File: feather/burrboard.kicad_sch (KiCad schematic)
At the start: 27 parts, among them J1 J1, J2 J2, J3 22-23-2021, Q1 TEMT6000X01, U1 TMP36, U2 ADXL345BCCZ

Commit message: Add BOM
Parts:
- removed J3: 22-23-2021, burrboard:PinHeader_1x2_P2.54mm, symbol dk_Rectangular-Connectors-Headers-Male-Pins:22-23-2021
- added J3: Conn_01x02_Male, Connector_PinHeader_2.54mm:PinHeader_1x02_P2.54mm_Vertical, symbol Connector:Conn_01x02_Male
- BT1: Digi-Key_PN (none) -> 36-2479-ND
- C1, C3, C4: Digi-Key_PN (none) -> 1276-1003-2-ND
- C2: Digi-Key_PN (none) -> 1276-2891-2-ND
- D1: AISLER_MPN APT2012LSECK/J3-PRV -> APT2012SECK/J3-PRV; Digi-Key_PN (none) -> 754-1791-2-ND; MPN APT2012LSECK/J3-PRV -> APT2012SECK/J3-PRV; Manufacturer https://www.digikey.no/en/products/detail/kingbright/APT201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 -> Kingbright
- D2: Digi-Key_PN (none) -> 754-1939-2-ND; Manufacturer https://www.digikey.no/en/products/detail/kingbright/APT201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 -> Kingbright
- D3: Digi-Key_PN (none) -> 754-1938-2-ND; Manufacturer https://www.digikey.no/en/products/detail/kingbright/APT201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 -> Kingbright
- D4: Digi-Key_PN (none) -> 754-1937-2-ND; Manufacturer https://www.digikey.no/en/products/detail/kingbright/APT201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 -> Kingbright
- J1: AISLER_MPN M20-7821642 -> PPTC161LFBN-RC; Digi-Key_PN (none) -> S7014-ND; MPN M20-7821642 -> PPTC161LFBN-RC; Manufacturer Harwin Inc -> Sullins Connector Solutions
- J2: AISLER_MPN M20-7821242 -> PPTC121LFBN-RC; Digi-Key_PN (none) -> S6100-ND; MPN M20-7821242 -> PPTC121LFBN-RC; Manufacturer Harwin Inc -> Sullins Connector Solutions
- R1, R2, R3, R4, R5: Digi-Key_PN (none) -> RMCF0805FT10K0TR-ND
- R6, R8: Digi-Key_PN (none) -> RMCF0805FT1K50TR-ND
- R7, R9: Digi-Key_PN (none) -> RMCF0805FT680RTR-ND
- U1: Digi-Key_PN (none) -> TMP36FSZ-ND
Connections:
- net VDD: now also J3.2 (Pin_2)
- net VUSB: now also J3.1 (Pin_1)

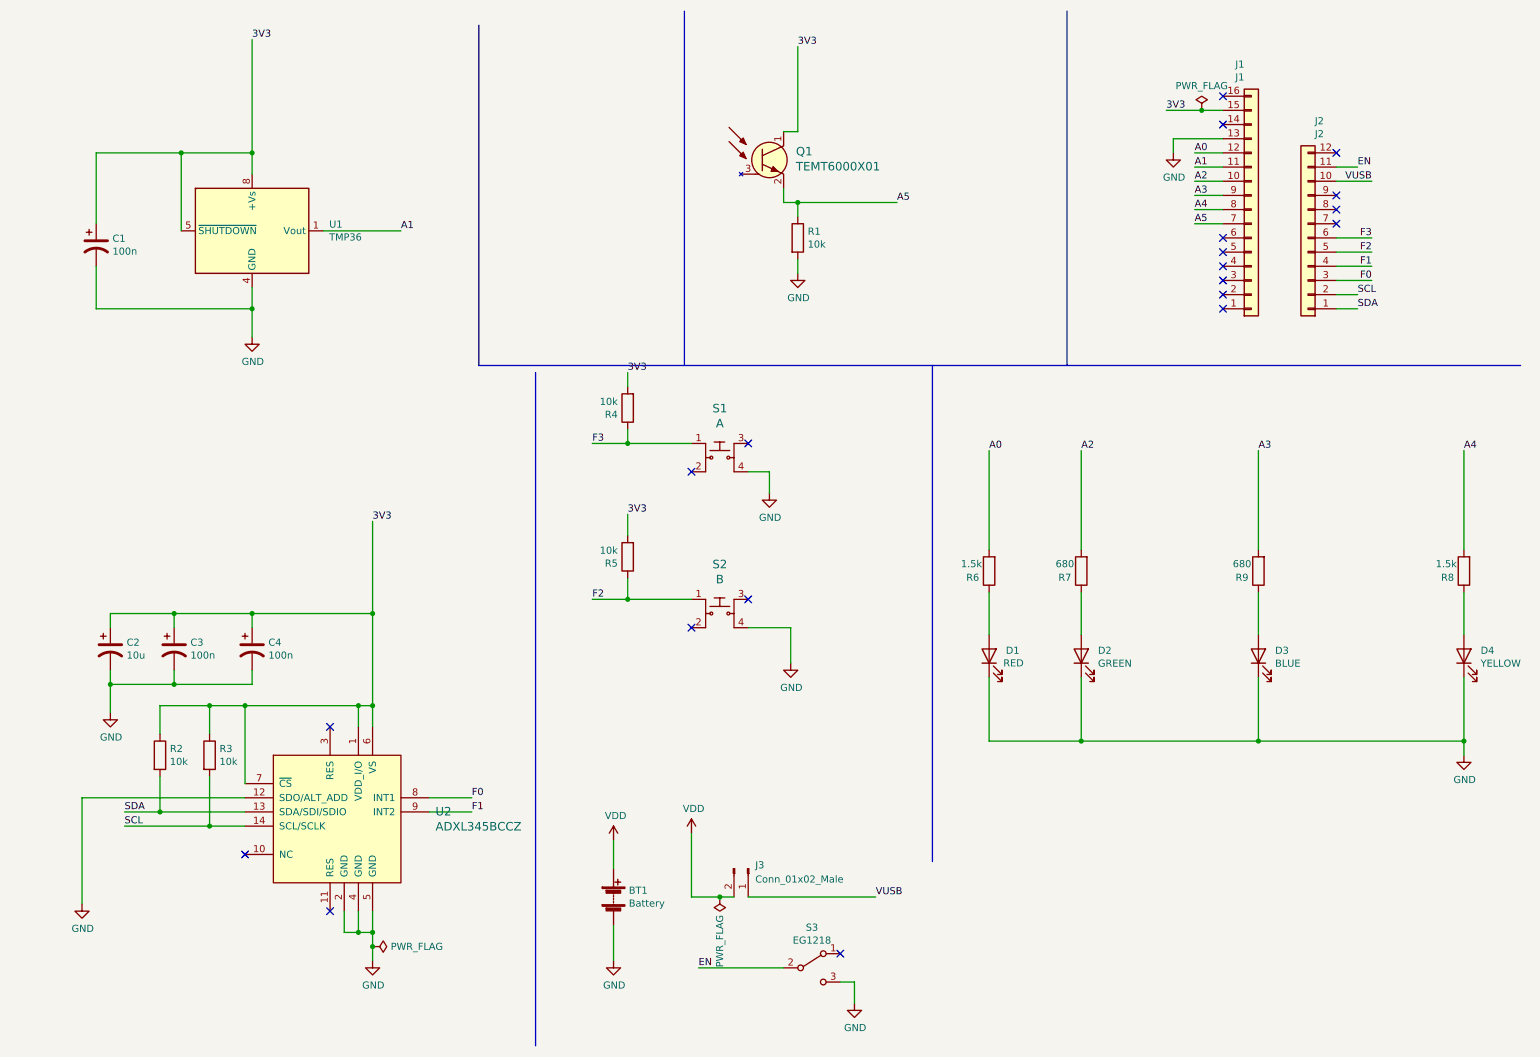
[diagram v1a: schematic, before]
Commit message: Update temt footprint
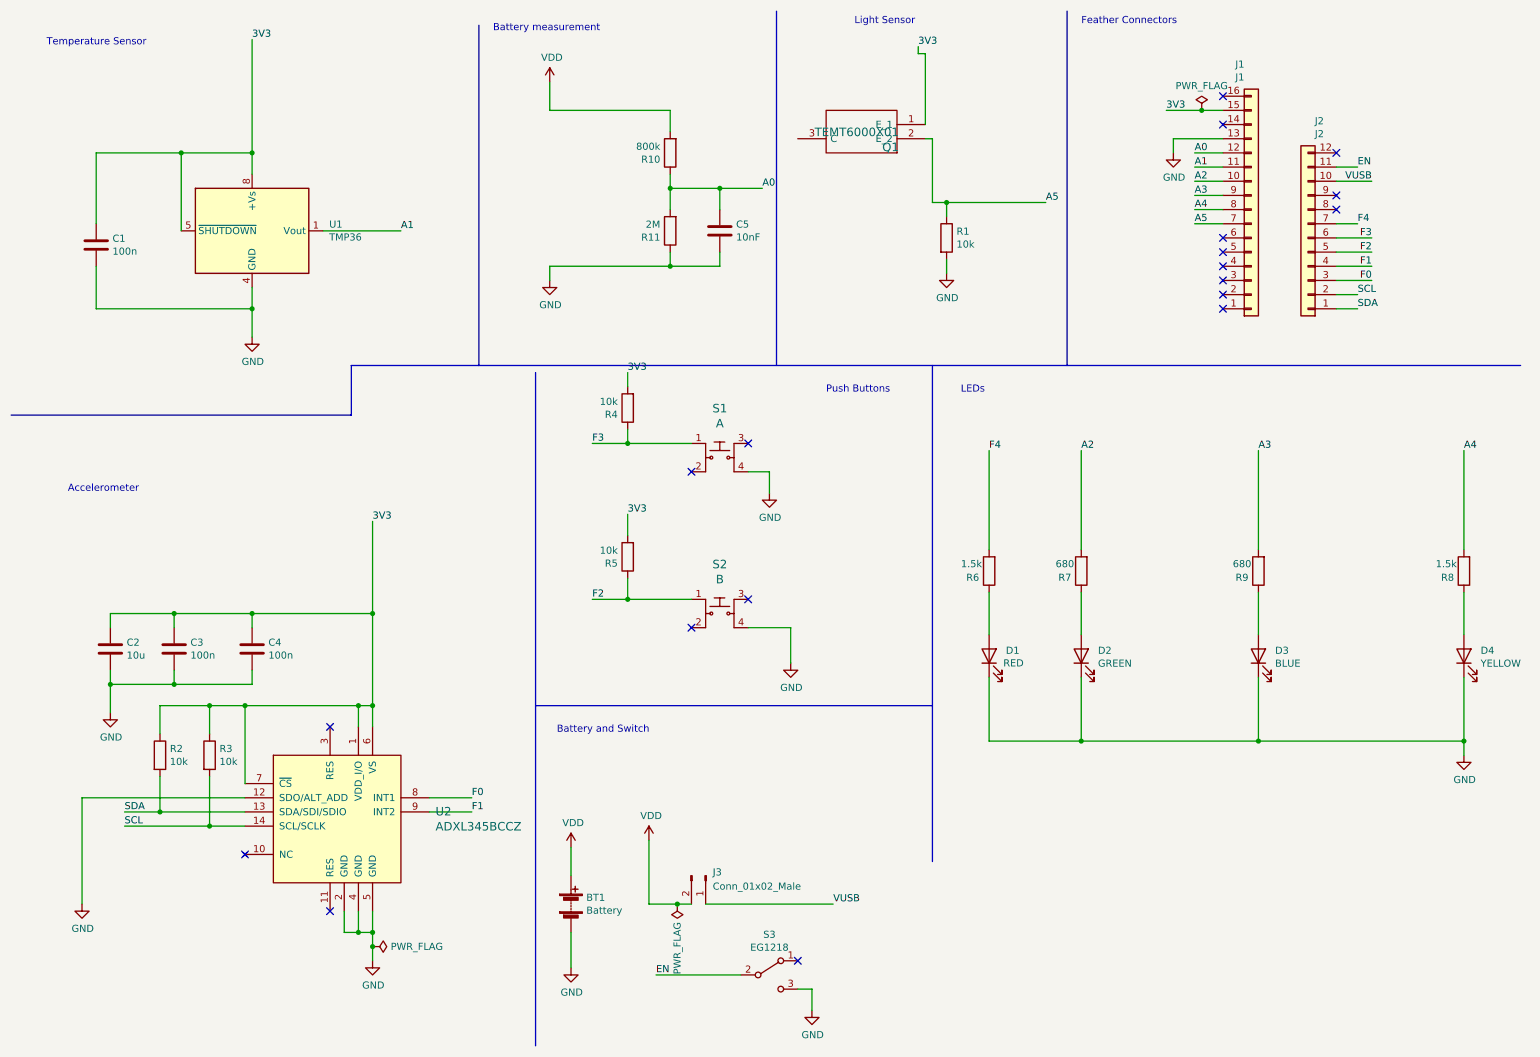
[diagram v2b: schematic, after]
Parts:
- added C5: 10nF, Capacitor_SMD:C_0805_2012Metric, symbol Device:C
- added R10: 800k, Resistor_SMD:R_0805_2012Metric, symbol Device:R
- added R11: 2M, Resistor_SMD:R_0805_2012Metric, symbol Device:R
- C1, C2, C3, C4: footprint Capacitor_SMD:C_0805_2012Metric_Pad1.18x1.45mm_HandSolder -> Capacitor_SMD:C_0805_2012Metric; symbol Device:CP1 -> Device:C
- D1, D2, D3, D4: footprint LED_SMD:LED_0805_2012Metric_Pad1.15x1.40mm_HandSolder -> LED_SMD:LED_0805_2012Metric
- Q1: footprint burrboard:Phototransistor_SMD_4x2mm_TEMT6000X01 -> TEMT6000X01; symbol dk_Optical-Sensors-Phototransistors:TEMT6000X01 -> burrboard:TEMT6000X01; Arrow Part Number (none) -> TEMT6000X01; Arrow Price/Stock (none) -> https://www.arrow.com/en/products/temt6000x01/vishay?region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; Manufacturer_Name (none) -> Vishay; Manufacturer_Part_Number (none) -> TEMT6000X01; Mouser Part Number (none) -> 78-TEMT6000; Mouser Price/Stock (none) -> https://www.mouser.co.uk/ProductDetail/Vishay-Semiconductor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
- R1, R2, R3, R4, R5, R6, R7, R8, R9: footprint Resistor_SMD:R_0805_2012Metric_Pad1.20x1.40mm_HandSolder -> Resistor_SMD:R_0805_2012Metric
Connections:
- net A0: now also C5.1, R10.1, R11.2; no longer R6.2
- net GND: now also C5.2, R11.1
- net VDD: now also R10.2
- net F4: now reaches J2.7 (Pin_7)
- net F4: now also R6.2
- no-connect marks 20 -> 19
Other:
- note added: "Accelerometer"
- note added: "Battery and Switch"
- note added: "Battery measurement"
- note added: "Feather Connectors"
- note added: "LEDs"
- note added: "Light Sensor"
- note added: "Push Buttons"
- note added: "Temperature Sensor"
- moved on the sheet: BT1, J3, R1, S3

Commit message: Fixup
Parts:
- Q1: footprint TEMT6000X01 -> burrboard:Phototransistor_SMD_4x2mm_TEMT6000X01
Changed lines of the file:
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@@
       (effects (font (size 1.524 1.524)) (justify left))
     )
-    (property "Footprint" "TEMT6000X01" (id 2) (at 157.48 38.1 0)
+    (property "Footprint" "burrboard:Phototransistor_SMD_4x2mm_TEMT6000X01" (id 2) (at 157.48 38.1 0)
       (effects (font (size 1.27 1.27)) (justify left) hide)
     )
@@
     )
     (path "/00000000-0000-0000-0000-000061ecf6dc"
-      (reference "Q1") (unit 1) (value "TEMT6000X01") (footprint "TEMT6000X01")
+      (reference "Q1") (unit 1) (value "TEMT6000X01") (footprint "burrboard:Phototransistor_SMD_4x2mm_TEMT6000X01")
     )
     (path "/00000000-0000-0000-0000-000061c212d9"

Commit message: Fix symbols
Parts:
- U2: footprint burrboard:LGA-14_3x5mm_RevA -> digikey-footprints:LGA-14_3x5mm_RevA; symbol dk_Motion-Sensors-Accelerometers:ADXL345BCCZ -> burrboard:ADXL345BCCZ
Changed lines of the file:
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@@
   (no_connect (at 134.62 123.19))
   (no_connect (at 250.19 48.26))
-  (no_connect (at 54.61 163.83))
   (no_connect (at 134.62 95.25))
   (no_connect (at 229.87 60.96))
+  (no_connect (at 153.67 35.56))
   (no_connect (at 229.87 33.02))
   (no_connect (at 229.87 66.04))
@@
     (pin "8")
   )
-  (symbol (lib_id "dk_Motion-Sensors-Accelerometers:ADXL345BCCZ") (at 69.85 156.21 0) (unit 1)
+  (symbol (lib_id "burrboard:ADXL345BCCZ") (at 69.85 156.21 0) (unit 1)
     (in_bom yes) (on_board yes)
     (property "Reference" "U2" (id 0) (at 88.7476 156.1338 0)
@@
       (effects (font (size 1.524 1.524)) (justify left))
     )
-    (property "Footprint" "burrboard:LGA-14_3x5mm_RevA" (id 2) (at 74.93 151.13 0)
+    (property "Footprint" "digikey-footprints:LGA-14_3x5mm_RevA" (id 2) (at 74.93 151.13 0)
       (effects (font (size 1.524 1.524)) (justify left) hide)
     )
@@
     )
     (path "/00000000-0000-0000-0000-000061d5dad5"
-      (reference "U2") (unit 1) (value "ADXL345BCCZ") (footprint "burrboard:LGA-14_3x5mm_RevA")
-    )
-  )
+      (reference "U2") (unit 1) (value "ADXL345BCCZ") (footprint "digikey-footprints:LGA-14_3x5mm_RevA")
+    )
+  )

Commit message: Fixup
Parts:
- S1, S2: symbol dk_Tactile-Switches:PTS645SM43SMTR92_LFS -> burrboard:PTS645SM43SMTR92_LFS
- U2: footprint digikey-footprints:LGA-14_3x5mm_RevA -> burrboard:LGA-14_3x5mm_RevA
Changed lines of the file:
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@@
       (effects (font (size 1.524 1.524)) (justify left))
     )
-    (property "Footprint" "digikey-footprints:LGA-14_3x5mm_RevA" (id 2) (at 74.93 151.13 0)
+    (property "Footprint" "burrboard:LGA-14_3x5mm_RevA" (id 2) (at 74.93 151.13 0)
       (effects (font (size 1.524 1.524)) (justify left) hide)
     )
@@
     (pin "1")
   )
-  (symbol (lib_id "dk_Tactile-Switches:PTS645SM43SMTR92_LFS") (at 139.7 92.71 0) (unit 1)
+  (symbol (lib_id "burrboard:PTS645SM43SMTR92_LFS") (at 139.7 92.71 0) (unit 1)
     (in_bom yes) (on_board yes)
     (property "Reference" "S1" (id 0) (at 139.7 83.8962 0)
@@
     (pin "4")
   )
-  (symbol (lib_id "dk_Tactile-Switches:PTS645SM43SMTR92_LFS") (at 139.7 120.65 0) (unit 1)
+  (symbol (lib_id "burrboard:PTS645SM43SMTR92_LFS") (at 139.7 120.65 0) (unit 1)
     (in_bom yes) (on_board yes)
     (property "Reference" "S2" (id 0) (at 139.7 111.8362 0)
@@
     )
     (path "/00000000-0000-0000-0000-000061d5dad5"
-      (reference "U2") (unit 1) (value "ADXL345BCCZ") (footprint "digikey-footprints:LGA-14_3x5mm_RevA")
-    )
-  )
+      (reference "U2") (unit 1) (value "ADXL345BCCZ") (footprint "burrboard:LGA-14_3x5mm_RevA")
+    )
+  )

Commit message: Update
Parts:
- removed Q1: TEMT6000X01, burrboard:Phototransistor_SMD_4x2mm_TEMT6000X01, symbol burrboard:TEMT6000X01
- added Q?: TEMT6000X01, burrboard:Phototransistor_SMD_4x2mm_TEMT6000X01, symbol burrboard:TEMT6000X01
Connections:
- net 3V3: now also Q?.3 (C)
- net A5: now also Q?.2 (E_2)
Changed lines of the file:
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@@
   (no_connect (at 134.62 95.25))
   (no_connect (at 229.87 60.96))
-  (no_connect (at 153.67 35.56))
+  (no_connect (at 180.34 43.18))
   (no_connect (at 229.87 33.02))
   (no_connect (at 229.87 66.04))
@@
     (stroke (width 0) (type default) (color 0 0 0 0))
   )
-  (wire (pts (xy 175.26 20.32) (xy 175.26 19.05))
-    (stroke (width 0) (type default) (color 0 0 0 0))
-  )
   (wire (pts (xy 132.08 172.72) (xy 134.62 172.72))
     (stroke (width 0) (type default) (color 0 0 0 0))
@@
     (stroke (width 0) (type default) (color 0 0 0 0))
   )
+  (wire (pts (xy 177.8 43.18) (xy 177.8 46.99))
+    (stroke (width 0) (type default) (color 0 0 0 0))
+  )
   (wire (pts (xy 109.22 30.48) (xy 130.81 30.48))
     (stroke (width 0) (type default) (color 0 0 0 0))
@@
     (stroke (width 0) (type default) (color 0 0 0 0))
   )
-  (wire (pts (xy 177.8 35.56) (xy 176.53 35.56))
-    (stroke (width 0) (type default) (color 0 0 0 0))
-  )
   (wire (pts (xy 55.88 62.23) (xy 55.88 66.04))
     (stroke (width 0) (type default) (color 0 0 0 0))
@@
     (stroke (width 0) (type default) (color 0 0 0 0))
   )
+  (wire (pts (xy 177.8 16.51) (xy 177.8 20.32))
+    (stroke (width 0) (type default) (color 0 0 0 0))
+  )
   (wire (pts (xy 229.87 43.18) (xy 224.79 43.18))
     (stroke (width 0) (type default) (color 0 0 0 0))
@@
     (stroke (width 0) (type default) (color 0 0 0 0))
   )
-  (wire (pts (xy 176.53 20.32) (xy 175.26 20.32))
-    (stroke (width 0) (type default) (color 0 0 0 0))
-  )
   (wire (pts (xy 273.05 132.08) (xy 273.05 143.51))
     (stroke (width 0) (type default) (color 0 0 0 0))
@@
     (stroke (width 0) (type default) (color 0 0 0 0))
   )
-  (wire (pts (xy 177.8 35.56) (xy 177.8 46.99))
-    (stroke (width 0) (type default) (color 0 0 0 0))
-  )
   (polyline (pts (xy 96.52 76.2) (xy 73.66 76.2))
     (stroke (width 0) (type default) (color 0 0 0 0))
@@
   )
   (wire (pts (xy 39.37 156.21) (xy 39.37 149.86))
-    (stroke (width 0) (type default) (color 0 0 0 0))
-  )
-  (wire (pts (xy 176.53 33.02) (xy 176.53 20.32))
     (stroke (width 0) (type default) (color 0 0 0 0))
   )
@@
     (effects (font (size 1.27 1.27)) (justify left bottom))
   )
-  (label "3V3" (at 175.26 19.05 0)
+  (label "3V3" (at 177.8 16.51 0)
     (effects (font (size 1.27 1.27)) (justify left bottom))
   )
@@
     (pin "2")
   )
-  (symbol (lib_id "burrboard:TEMT6000X01") (at 176.53 35.56 180) (unit 1)
-    (in_bom yes) (on_board yes)
-    (property "Reference" "Q1" (id 0) (at 171.7802 37.084 0)
-      (effects (font (size 1.524 1.524)) (justify left))
-    )
-    (property "Value" "TEMT6000X01" (id 1) (at 171.7802 34.3916 0)
-      (effects (font (size 1.524 1.524)) (justify left))
-    )
-    (property "Footprint" "burrboard:Phototransistor_SMD_4x2mm_TEMT6000X01" (id 2) (at 157.48 38.1 0)
-      (effects (font (size 1.27 1.27)) (justify left) hide)
-    )
-    (property "Datasheet" "https://www.vishay.com/docs/81579/temt6000.pdf" (id 3) (at 157.48 35.56 0)
-      (effects (font (size 1.27 1.27)) (justify left) hide)
-    )
-    (property "Digi-Key_PN" "751-1055-1-ND" (id 4) (at 171.45 45.72 0)
-      (effects (font (size 1.524 1.524)) (justify left) hide)
-    )
-    (property "MPN" "TEMT6000X01" (id 5) (at 171.45 48.26 0)
-      (effects (font (size 1.524 1.524)) (justify left) hide)
-    )
-    (property "Category" "Sensors, Transducers" (id 6) (at 171.45 50.8 0)
-      (effects (font (size 1.524 1.524)) (justify left) hide)
-    )
-    (property "Family" "Optical Sensors - Phototransistors" (id 7) (at 171.45 53.34 0)
-      (effects (font (size 1.524 1.524)) (justify left) hide)
-    )
-    (property "DK_Datasheet_Link" "http://www.vishay.com/docs/81579/temt6000.pdf" (id 8) (at 171.45 55.88 0)
-      (effects (font (size 1.524 1.524)) (justify left) hide)
-    )
-    (property "DK_Detail_Page" "/product-detail/en/vishay-semiconductor-opto-division/TEMT6000X01/751-1055-1-ND/1681410" (id 9) (at 171.45 58.42 0)
-      (effects (font (size 1.524 1.524)) (justify left) hide)
-    )
-    (property "Description" "Ambient Light Sensor 570nm SMD3 Vishay TEMT6000X01 +/-60  Visible Light Phototransistor, Surface Mount 3-Pin 1206 package" (id 10) (at 157.48 33.02 0)
-      (effects (font (size 1.27 1.27)) (justify left) hide)
-    )
-    (property "Manufacturer" "Vishay Semiconductor Opto Division" (id 11) (at 171.45 63.5 0)
-      (effects (font (size 1.524 1.524)) (justify left) hide)
-    )
-    (property "Status" "Active" (id 12) (at 171.45 66.04 0)
-      (effects (font (size 1.524 1.524)) (justify left) hide)
-    )
-    (property "AISLER_MPN" "TEMT6000X01" (id 13) (at 176.53 35.56 0)
-      (effects (font (size 1.27 1.27)) hide)
-    )
-    (property "Height" "" (id 14) (at 157.48 30.48 0)
-      (effects (font (size 1.27 1.27)) (justify left) hide)
-    )
-    (property "Manufacturer_Name" "Vishay" (id 15) (at 157.48 27.94 0)
-      (effects (font (size 1.27 1.27)) (justify left) hide)
-    )
-    (property "Manufacturer_Part_Number" "TEMT6000X01" (id 16) (at 157.48 25.4 0)
-      (effects (font (size 1.27 1.27)) (justify left) hide)
-    )
-    (property "Mouser Part Number" "78-TEMT6000" (id 17) (at 157.48 22.86 0)
-      (effects (font (size 1.27 1.27)) (justify left) hide)
-    )
-    (property "Mouser Price/Stock" "https://www.mouser.co.uk/ProductDetail/Vishay-Semiconductors/TEMT6000X01?qs=%2Fjqivxn91ccZGXDwz0wGxg%3D%3D" (id 18) (at 157.48 20.32 0)
-      (effects (font (size 1.27 1.27)) (justify left) hide)
-    )
-    (property "Arrow Part Number" "TEMT6000X01" (id 19) (at 157.48 17.78 0)
-      (effects (font (size 1.27 1.27)) (justify left) hide)
-    )
-    (property "Arrow Price/Stock" "https://www.arrow.com/en/products/temt6000x01/vishay?region=nac" (id 20) (at 157.48 15.24 0)
-      (effects (font (size 1.27 1.27)) (justify left) hide)
-    )
-    (pin "1")
-    (pin "2")
-    (pin "3")
-  )
   (symbol (lib_id "Switch:SW_SPDT") (at 148.59 185.42 0) (unit 1)
     (in_bom yes) (on_board yes)
@@
     (pin "2")
   )
+  (symbol (lib_id "burrboard:TEMT6000X01") (at 177.8 43.18 90) (unit 1)
+    (in_bom yes) (on_board yes) (fields_autoplaced)
+    (property "Reference" "Q?" (id 0) (at 184.15 30.4799 90)
+      (effects (font (size 1.27 1.27)) (justify right))
+    )
+    (property "Value" "TEMT6000X01" (id 1) (at 184.15 33.0199 90)
+      (effects (font (size 1.27 1.27)) (justify right))
+    )
+    (property "Footprint" "burrboard:Phototransistor_SMD_4x2mm_TEMT6000X01" (id 2) (at 175.26 24.13 0)
+      (effects (font (size 1.27 1.27)) (justify left) hide)
+    )
+    (property "Datasheet" "https://www.vishay.com/docs/81579/temt6000.pdf" (id 3) (at 177.8 24.13 0)
+      (effects (font (size 1.27 1.27)) (justify left) hide)
+    )
+    (property "Description" "Ambient Light Sensor 570nm SMD3 Vishay TEMT6000X01 +/-60  Visible Light Phototransistor, Surface Mount 3-Pin 1206 package" (id 4) (at 180.34 24.13 0)
+      (effects (font (size 1.27 1.27)) (justify left) hide)
+    )
+    (property "Height" "" (id 5) (at 182.88 24.13 0)
+      (effects (font (size 1.27 1.27)) (justify left) hide)
+    )
+    (property "Manufacturer_Name" "Vishay" (id 6) (at 185.42 24.13 0)
+      (effects (font (size 1.27 1.27)) (justify left) hide)
+    )
+    (property "Manufacturer_Part_Number" "TEMT6000X01" (id 7) (at 187.96 24.13 0)
+      (effects (font (size 1.27 1.27)) (justify left) hide)
+    )
+    (property "Mouser Part Number" "78-TEMT6000" (id 8) (at 190.5 24.13 0)
+      (effects (font (size 1.27 1.27)) (justify left) hide)
+    )
+    (property "Mouser Price/Stock" "https://www.mouser.co.uk/ProductDetail/Vishay-Semiconductors/TEMT6000X01?qs=%2Fjqivxn91ccZGXDwz0wGxg%3D%3D" (id 9) (at 193.04 24.13 0)
+      (effects (font (size 1.27 1.27)) (justify left) hide)
+    )
+    (property "Arrow Part Number" "TEMT6000X01" (id 10) (at 195.58 24.13 0)
+      (effects (font (size 1.27 1.27)) (justify left) hide)
+    )
+    (property "Arrow Price/Stock" "https://www.arrow.com/en/products/temt6000x01/vishay?region=nac" (id 11) (at 198.12 24.13 0)
+      (effects (font (size 1.27 1.27)) (justify left) hide)
+    )
+    (pin "1")
+    (pin "2")
+    (pin "3")
+  )
   (symbol (lib_id "Device:C") (at 139.7 52.07 0) (unit 1)
     (in_bom yes) (on_board yes)
@@
       (reference "J3") (unit 1) (value "Conn_01x02_Male") (footprint "Connector_PinHeader_2.54mm:PinHeader_1x02_P2.54mm_Vertical")
     )
-    (path "/00000000-0000-0000-0000-000061ecf6dc"
-      (reference "Q1") (unit 1) (value "TEMT6000X01") (footprint "burrboard:Phototransistor_SMD_4x2mm_TEMT6000X01")
+    (path "/666dc925-2b95-4de4-a148-45e51fb4be3f"
+      (reference "Q?") (unit 1) (value "TEMT6000X01") (footprint "burrboard:Phototransistor_SMD_4x2mm_TEMT6000X01")
     )
     (path "/00000000-0000-0000-0000-000061c212d9"
